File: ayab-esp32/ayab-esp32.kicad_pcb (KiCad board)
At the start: 4 copper layers, 285.1 x 48.1 mm, 228 parts, among them J201 SPARE1, J202 SPARE0, J401 900.965.CK35 SOLENOIDS A, J402 900.965.CK35 SOLENOIDS B, J403 910.950 SOLENOIDS A, J404 910.950 SOLENOIDS B, J405 910.950 ENCODERS EOL R, J406 930.940 SOLENOIDS A, J407 930.940 SOLENOIDS B, J408 910.950 EOL L, J409 930.940 EOL R, J410 930.940 ENCODERS, J411 900.965 EOL L, J412 900.965 EOL R, J413 900.965 ENCODERS, J414 930.940 EOL L, J501 USB_C_Receptacle_USB2.0, J601 VIN, J602 Brother_5P, J604 Brother_4R, J701 CTRL_3v3, J702 CTRL_5V, J801 AYAB_UART, J802 I2C_VBUS, J803 USER_I2C, J804 I2C_VBUS, J805 AYAB_SPI, J806 AYAB_I2C, Q201 AO3400A, Q501 BCM857BV, Q502 LP9435LT1G, Q801 AO3400A, Q802 AO3400A, Q803 AO3400A, Q804 AO3400A, SW201 USER, SW202 RESET, SW203 BOOTSEL, U201 ESP32-S3-MINI-1, U301 MCP23017_SS, U302 ULN2003A, U303 ULN2003A, U304 ULN2003A, U501 SRV05-4, U601 XL1509, U602 XL1509, U701 SN74LVC4245

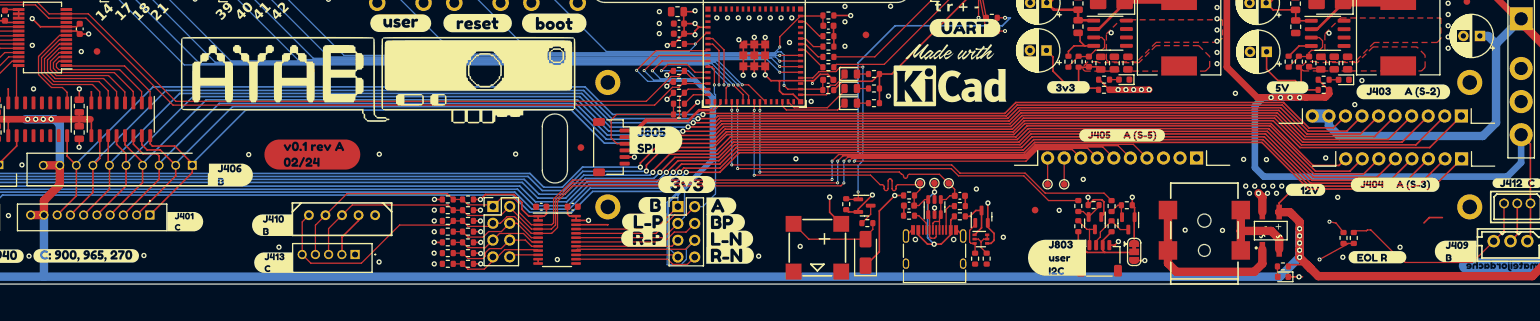
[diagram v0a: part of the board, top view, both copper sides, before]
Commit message: Apply validated KH910 solenoid power partition
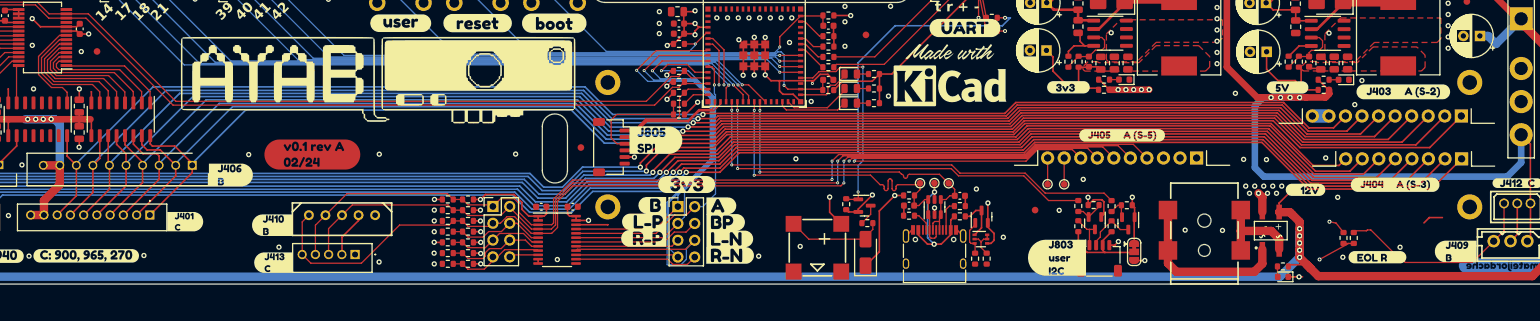
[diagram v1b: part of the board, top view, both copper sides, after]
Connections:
- C302 pad 1: +12V -> SOLENOID_12V_SW
- C303 pad 1: +12V -> SOLENOID_12V_SW
- C304 pad 1: +12V -> SOLENOID_12V_SW
- C603 pad 1: +12V -> SOLENOID_12V_SW
- C604 pad 1: +12V -> SOLENOID_12V_SW
- C605 pad 1: +12V -> SOLENOID_12V_SW
- J401 pad 10: +12V -> SOLENOID_12V_SW
- J401 pad 9: +12V -> SOLENOID_12V_SW
- J403 pad 10: +12V -> SOLENOID_12V_SW
- J403 pad 9: +12V -> SOLENOID_12V_SW
- J406 pad 10: +12V -> SOLENOID_12V_SW
- J406 pad 9: +12V -> SOLENOID_12V_SW
- U302 pad 9: +12V -> SOLENOID_12V_SW
- U303 pad 9: +12V -> SOLENOID_12V_SW
- U304 pad 9: +12V -> SOLENOID_12V_SW
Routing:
- net SOLENOID_12V_SW: track 0.00 -> 336.2 mm, vias 0 -> 4
- net +12V: track 540.2 -> 421.9 mm, vias 9 -> 5

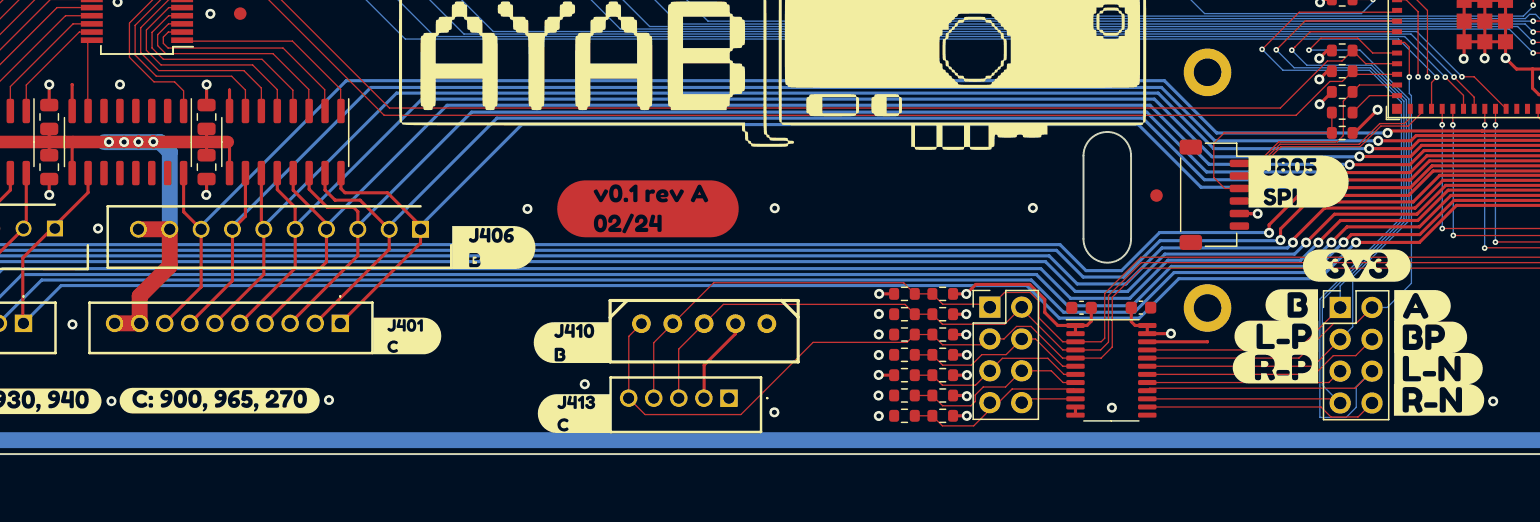
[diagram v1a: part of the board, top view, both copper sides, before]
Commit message: Integrate Rev A solenoid fail-safe gate
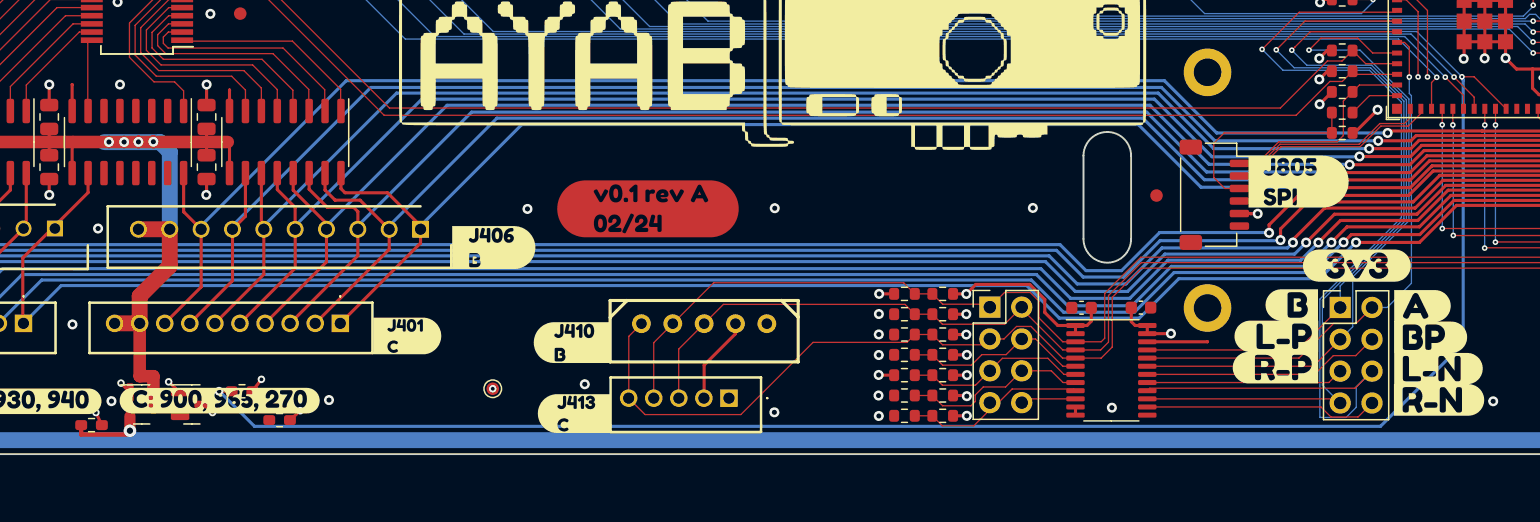
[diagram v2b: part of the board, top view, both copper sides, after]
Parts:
- added Q805: LP9435LT1G, Package_TO_SOT_SMD:SOT-23, F.Cu at (117.0, 160.2)
- added Q806: AO3400A, Package_TO_SOT_SMD:SOT-23, F.Cu at (121.0, 160.2)
- added R820: 100k, Resistor_SMD:R_0603_1608Metric, F.Cu at (113.0, 161.9)
- added R821: 10k, Resistor_SMD:R_0603_1608Metric, F.Cu at (125.0, 159.2)
- added R822: 100k, Resistor_SMD:R_0603_1608Metric, F.Cu at (128.0, 161.5)
- added TP703: SOL12_SW, TestPoint:TestPoint_Pad_D1.0mm, F.Cu at (145.0, 159.0)
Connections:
- net /ESP32/ESP21 renamed SOLENOID_PWR_EN
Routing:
- net SOLENOID_PWR_EN: track 98.4 -> 223.8 mm, vias 1 -> 2
- net SOLENOID_12V_SW: track 336.2 -> 374.2 mm, vias 4 -> 5
- net Net-(Q805-G): track 0.00 -> 15.1 mm, vias 0 -> 3
- net Net-(Q806-G): track 0.00 -> 14.9 mm, vias 0 -> 3
- net +12V: track 421.9 -> 429.9 mm, vias 5 -> 6

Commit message: Integrate Rev A protected power and sense routing
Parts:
- removed R611: 0R, Resistor_SMD:R_0603_1608Metric
- added R215: 47k, Resistor_SMD:R_0603_1608Metric, B.Cu at (225.0, 159.0)
- added R216: 10k, Resistor_SMD:R_0603_1608Metric, B.Cu at (228.5, 159.0)
- added U403: LM66100DCKR, Package_TO_SOT_SMD:SOT-363_SC-70-6, B.Cu at (300.0, 155.0)
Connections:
- U201 pad 8: /ESP32/EOL_R_N -> /ESP32/MACHINE_PWR_SENSE
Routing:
- net /ESP32/MACHINE_PWR_SENSE: track 0.00 -> 63.4 mm, vias 0 -> 2
- net /ESP32/EOL_R_N: track 65.3 -> 15.5 mm, vias 1 -> 0
- net /PSU/5V_SW: track 16.9 -> 58.9 mm, vias 0 -> 1
- net +5V: track 554.8 -> 573.3 mm
- net +12V: track 429.9 -> 434.0 mm
- net GND: track 139.3 -> 141.2 mm
